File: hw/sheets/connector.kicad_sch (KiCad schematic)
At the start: 1 part, among them J1 AH58893-T9B10-3F

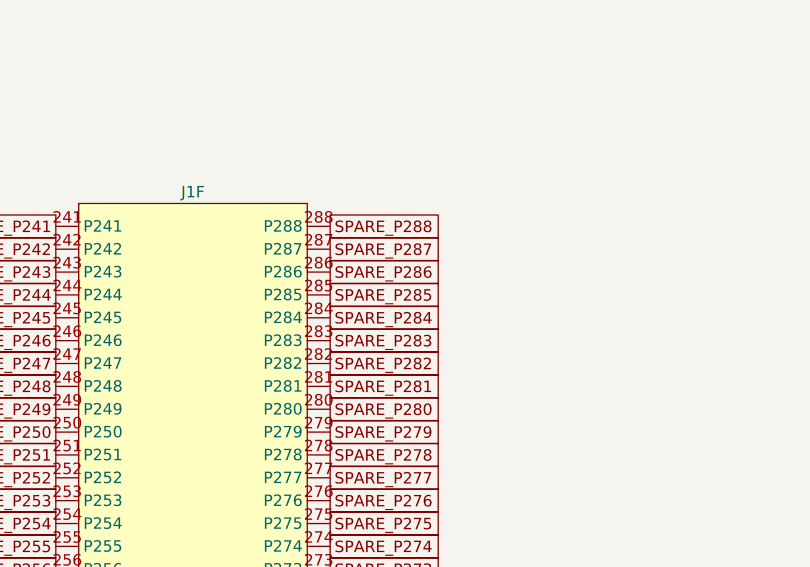
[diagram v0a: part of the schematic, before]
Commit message: Add MSC1 breakout (J37), ground J35 spare pads, add audio amp/mic tap (J38)
Carve J35's last 6 pins into a new MSC1 header (J37: CLK/CMD/D0-D3_CD),
keeping J35 at a fixed 26-pin size in both schematic and PCB with the
now-orphaned pads tied to GND. Add a 3-pin tap (J38) off the audio jack
(HPOUTL/GND/MICLP) so an external amplifier or mic can be wired in
directly instead of needing a breakout cable off J6.
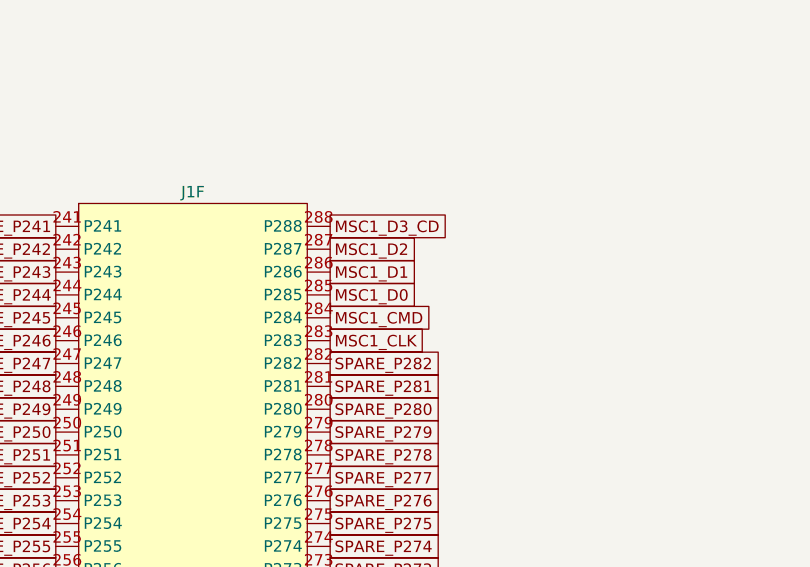
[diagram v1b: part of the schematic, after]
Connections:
- net SPARE_P283 renamed MSC1_CLK
- net SPARE_P284 renamed MSC1_CMD
- net SPARE_P285 renamed MSC1_D0
- net SPARE_P286 renamed MSC1_D1
- net SPARE_P287 renamed MSC1_D2
- net SPARE_P288 renamed MSC1_D3_CD
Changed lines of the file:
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@@
 	(global_label "SPARE_P281" (at 243.84 153.67 0) (effects (font (size 1.27 1.27)) (justify left)))
 	(global_label "SPARE_P282" (at 243.84 151.13 0) (effects (font (size 1.27 1.27)) (justify left)))
-	(global_label "SPARE_P283" (at 243.84 148.59 0) (effects (font (size 1.27 1.27)) (justify left)))
-	(global_label "SPARE_P284" (at 243.84 146.05 0) (effects (font (size 1.27 1.27)) (justify left)))
-	(global_label "SPARE_P285" (at 243.84 143.51 0) (effects (font (size 1.27 1.27)) (justify left)))
-	(global_label "SPARE_P286" (at 243.84 140.97 0) (effects (font (size 1.27 1.27)) (justify left)))
-	(global_label "SPARE_P287" (at 243.84 138.43 0) (effects (font (size 1.27 1.27)) (justify left)))
-	(global_label "SPARE_P288" (at 243.84 135.89 0) (effects (font (size 1.27 1.27)) (justify left)))
+	(global_label "MSC1_CLK" (at 243.84 148.59 0) (effects (font (size 1.27 1.27)) (justify left)))
+	(global_label "MSC1_CMD" (at 243.84 146.05 0) (effects (font (size 1.27 1.27)) (justify left)))
+	(global_label "MSC1_D0" (at 243.84 143.51 0) (effects (font (size 1.27 1.27)) (justify left)))
+	(global_label "MSC1_D1" (at 243.84 140.97 0) (effects (font (size 1.27 1.27)) (justify left)))
+	(global_label "MSC1_D2" (at 243.84 138.43 0) (effects (font (size 1.27 1.27)) (justify left)))
+	(global_label "MSC1_D3_CD" (at 243.84 135.89 0) (effects (font (size 1.27 1.27)) (justify left)))
 	(sheet_instances
 		(path "/016abe51-c097-4611-854e-0af763646499"
